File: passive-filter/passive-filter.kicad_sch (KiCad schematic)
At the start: 18 parts, among them J1 AudioJack2_Switch, J2 AudioJack2_Switch, J3 Conn_01x03, J4 Conn_01x03, U1 LM318N

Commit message: passive-filter: Set footprints
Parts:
- C1, C2: footprint (none) -> Capacitor_THT:CP_Axial_L18.0mm_D10.0mm_P25.00mm_Horizontal
- C3: footprint (none) -> Capacitor_THT:C_Disc_D5.0mm_W2.5mm_P5.00mm
- J1, J2: footprint (none) -> Connector_Audio:Jack_6.35mm_Neutrik_NMJ4HHD2_Horizontal
- J3, J4: footprint (none) -> Connector_JST:JST_PH_B3B-PH-K_1x03_P2.00mm_Vertical
- U1: footprint (none) -> Package_DIP:DIP-8_W7.62mm_Socket_LongPads
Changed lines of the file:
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@@
 			)
 		)
-		(property "Footprint" ""
+		(property "Footprint" "Capacitor_THT:CP_Axial_L18.0mm_D10.0mm_P25.00mm_Horizontal"
 			(at 51.7652 107.95 0)
 			(effects
@@
 			)
 		)
-		(property "Footprint" ""
+		(property "Footprint" "Connector_JST:JST_PH_B3B-PH-K_1x03_P2.00mm_Vertical"
 			(at 27.94 99.06 0)
 			(effects
@@
 			)
 		)
-		(property "Footprint" ""
+		(property "Footprint" "Capacitor_THT:CP_Axial_L18.0mm_D10.0mm_P25.00mm_Horizontal"
 			(at 51.7652 97.79 0)
 			(effects
@@
 			)
 		)
-		(property "Footprint" ""
+		(property "Footprint" "Connector_JST:JST_PH_B3B-PH-K_1x03_P2.00mm_Vertical"
 			(at 143.51 100.33 0)
 			(effects
@@
 			)
 		)
-		(property "Footprint" ""
+		(property "Footprint" "Capacitor_THT:C_Disc_D5.0mm_W2.5mm_P5.00mm"
 			(at 127.9652 35.56 0)
 			(effects
@@
 			)
 		)
-		(property "Footprint" ""
+		(property "Footprint" "Connector_Audio:Jack_6.35mm_Neutrik_NMJ4HHD2_Horizontal"
 			(at 29.21 46.99 0)
 			(effects
@@
 			)
 		)
-		(property "Footprint" ""
+		(property "Footprint" "Package_DIP:DIP-8_W7.62mm_Socket_LongPads"
 			(at 118.11 41.91 0)
 			(effects
@@
 			)
 		)
-		(property "Footprint" ""
+		(property "Footprint" "Connector_Audio:Jack_6.35mm_Neutrik_NMJ4HHD2_Horizontal"
 			(at 146.05 46.99 0)
 			(effects

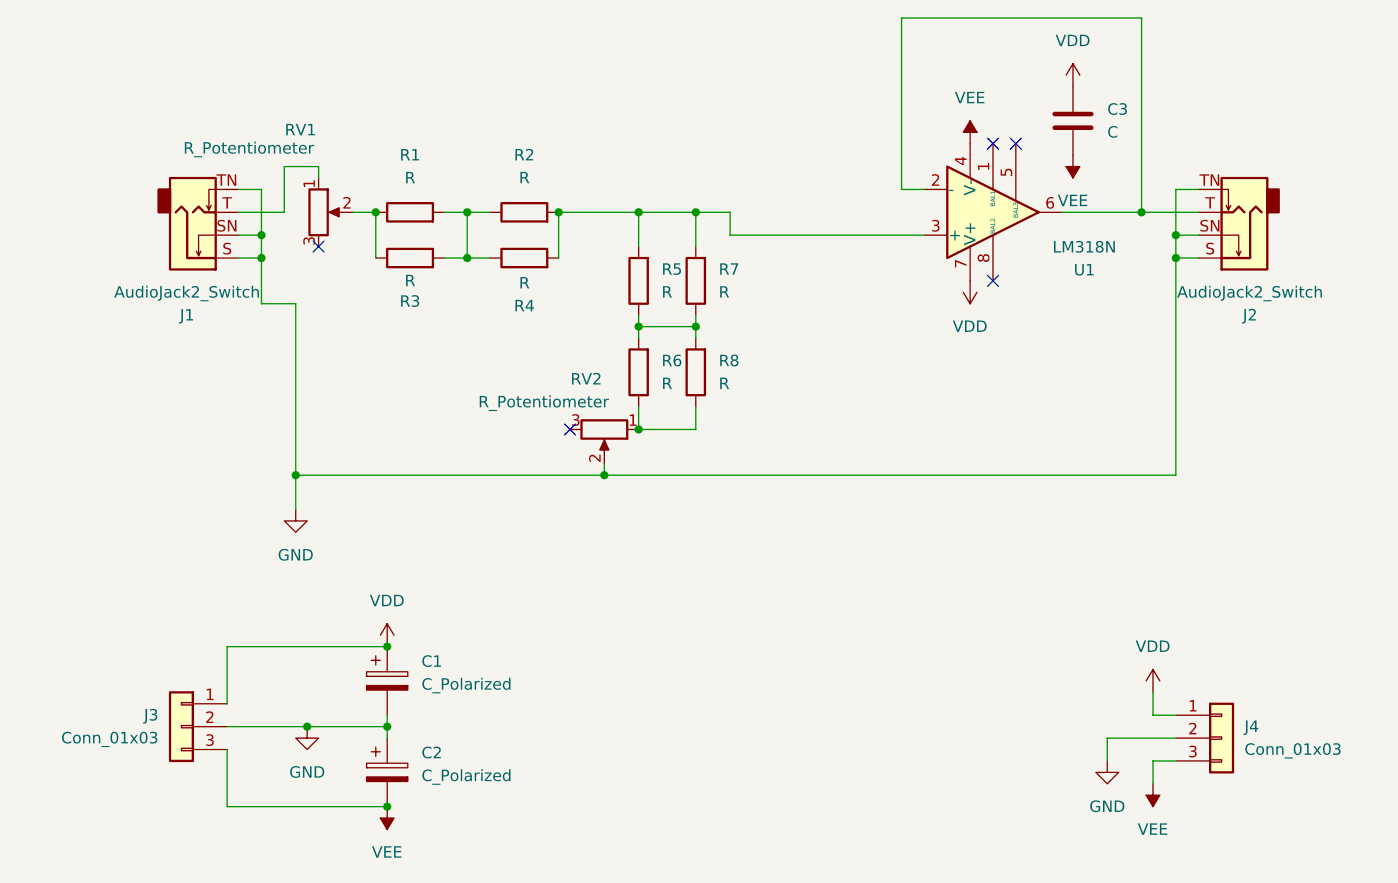
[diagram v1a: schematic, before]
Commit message: passive-filter: Add PCB
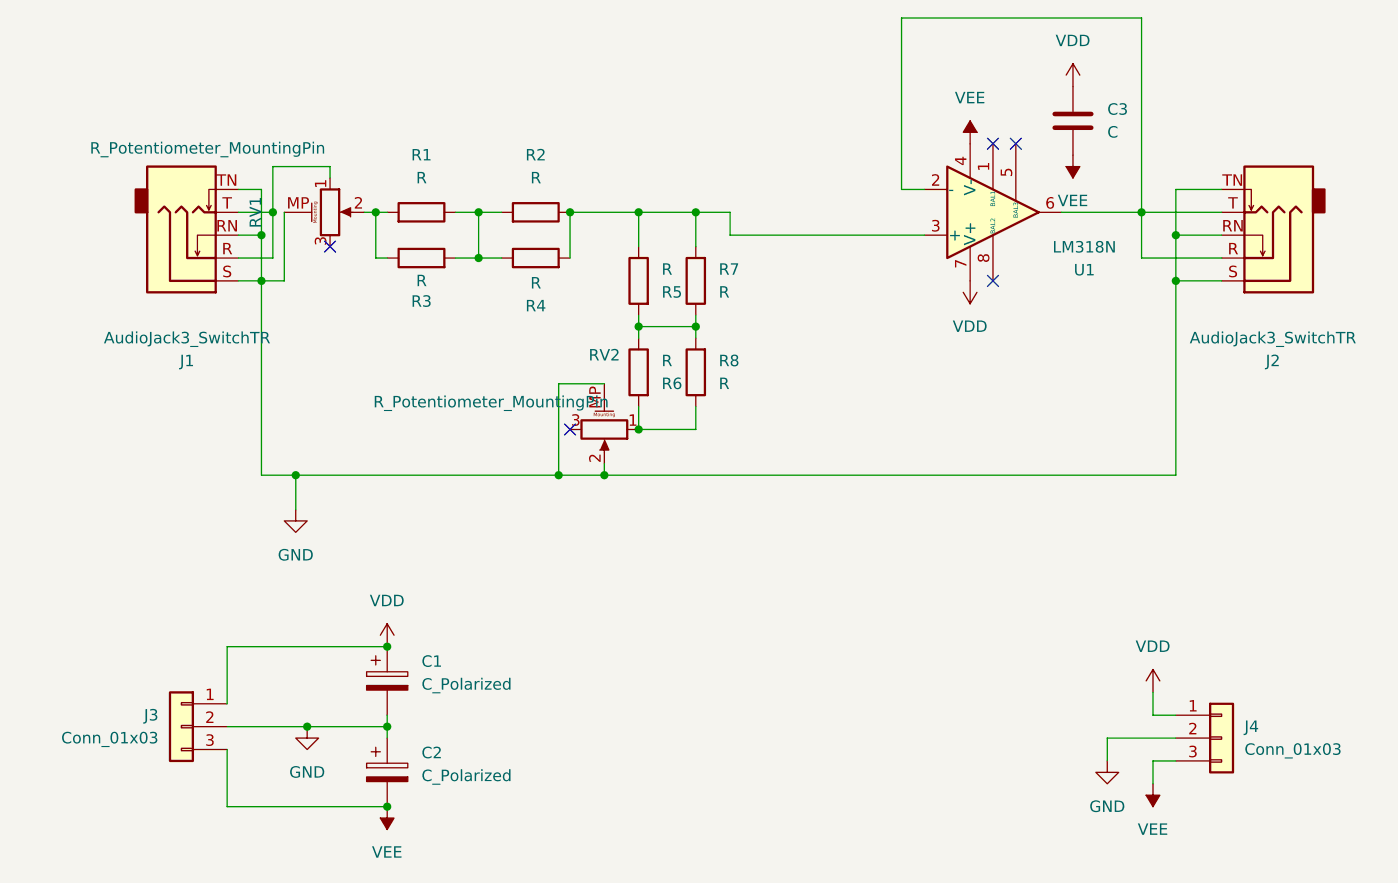
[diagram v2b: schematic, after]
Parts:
- C1, C2: footprint Capacitor_THT:CP_Axial_L18.0mm_D10.0mm_P25.00mm_Horizontal -> Capacitor_THT:CP_Radial_D10.0mm_P5.00mm
- J1, J2: value AudioJack2_Switch -> AudioJack3_SwitchTR; footprint Connector_Audio:Jack_6.35mm_Neutrik_NMJ4HHD2_Horizontal -> Connector_Audio:Jack_3.5mm_CUI_SJ1-3525N_Horizontal; symbol Connector_Audio:AudioJack2_Switch -> Connector_Audio:AudioJack3_SwitchTR
- RV1, RV2: value R_Potentiometer -> R_Potentiometer_MountingPin; symbol Device:R_Potentiometer -> Device:R_Potentiometer_MountingPin
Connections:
- net GND: now also J1.RN, J2.RN, RV1.MP (MountPin), RV2.MP (MountPin); no longer J1.SN, J2.SN
- net at R7.1, R8.2: now also R5.2, R6.1; no longer R5.1, R6.2
- net at R4.2, R7.2, U1.3 (+): now also R2.1, R5.1; no longer R2.2, R5.2
- net at R8.1, RV2.1: now also R6.2; no longer R6.1
- net at R3.2, R4.1: now also R1.1, R2.2; no longer R1.2, R2.1
- net at R3.1, RV1.2: now also R1.2; no longer R1.1
- net at J1.T, RV1.1: now also J1.R
- net at J2.T, U1.2 (-), U1.6: now also J2.R
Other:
- moved on the sheet: R1, R2, R3, R4, R5, R6

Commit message: passive-filter: Add PCB v2
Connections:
- net VDD: now also C3.2; no longer C3.1
- net VEE: now also C3.1; no longer C3.2
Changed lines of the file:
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@@
 		(lib_id "Device:C")
 		(at 127 31.75 0)
+		(mirror x)
 		(unit 1)
 		(exclude_from_sim no)
@@
 		(on_board yes)
 		(dnp no)
-		(fields_autoplaced yes)
 		(property "Reference" "C3"
-			(at 130.81 30.4799 0)
+			(at 130.81 33.0201 0)
 			(effects
 				(font
@@
 		)
 		(property "Value" "C"
-			(at 130.81 33.0199 0)
+			(at 130.81 30.4801 0)
 			(effects
 				(font
@@
 		)
 		(property "Footprint" "Capacitor_THT:C_Disc_D5.0mm_W2.5mm_P5.00mm"
-			(at 127.9652 35.56 0)
+			(at 127.9652 27.94 0)
 			(effects
 				(font
